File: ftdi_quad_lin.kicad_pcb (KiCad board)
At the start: 2 copper layers, 55 x 80 mm, 142 parts, among them J1 USB_C_Receptacle_USB2.0_16P, J2 Screw_Terminal_01x03, J3 Screw_Terminal_01x03, J4 Screw_Terminal_01x03, J5 Screw_Terminal_01x03, J6 Conn_01x10, J7 Conn_01x05, J8 Barrel_Jack_MountingPin, Q1 MMBT2222A, Q10 MMBT2222A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

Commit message: pulldown reset
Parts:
- added R46: 100k, Resistor_SMD:R_0805_2012Metric, F.Cu at (100.2, 98.7)
- D10, D11, D12, D13: footprint Diode_SMD:D_SOD-323 -> Diode_SMD:D_SOD-323_HandSoldering
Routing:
- net Net-(JP9-A): track 6.77 -> 9.76 mm
- net GND: vias 118 -> 117

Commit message: fixin mes g
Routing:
- net GND: track 127.7 -> 131.6 mm, vias 117 -> 120
- net /LIN0_TXD: track 54.2 -> 56.5 mm
- net Net-(D15-K): track 61.5 -> 59.8 mm
- net /LIN0_RXD: track 52.8 -> 53.4 mm
- net /LIN2_TXD: track 66.0 -> 65.8 mm, vias 4 -> 2

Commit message: power checked
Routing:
- net +5V: track 274.6 -> 283.5 mm
- net Net-(D15-K): track 59.8 -> 59.2 mm
- net GND: track 131.6 -> 131.3 mm, vias 120 -> 116
- added copper zone on F.Cu, net +12V
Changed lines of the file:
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@@
 	)
 	(segment
+		(start 86.6 65.275)
+		(end 85.1 66.775)
+		(width 0.5)
+		(layer "F.Cu")
+		(net 8)
+	)
+	(segment
 		(start 109.225 73)
 		(end 110.049311 72.175689)
@@
 	)
 	(segment
+		(start 93.35 65.275)
+		(end 91.3875 65.275)
+		(width 0.5)
+		(layer "F.Cu")
+		(net 8)
+	)
+	(segment
 		(start 97.36759 85.08241)
 		(end 97.1 85.35)
@@
 	)
 	(segment
+		(start 91.3875 65.275)
+		(end 89.8875 66.775)
+		(width 0.5)
+		(layer "F.Cu")
+		(net 8)
+	)
+	(segment
 		(start 94.86759 88.08241)
 		(end 97.36759 90.58241)
@@
 	)
 	(segment
-		(start 91.3875 65.275)
-		(end 89.8875 66.775)
-		(width 0.2)
-		(layer "F.Cu")
-		(net 8)
-	)
-	(segment
 		(start 119.1 94.121249)
 		(end 119.1 91.48625)
@@
 	)
 	(segment
-		(start 93.35 65.275)
-		(end 91.3875 65.275)
-		(width 0.2)
-		(layer "F.Cu")
-		(net 8)
-	)
-	(segment
 		(start 85.1 66.775)
 		(end 84.14491 67.73009)
@@
 	)
 	(segment
+		(start 93.35 65.275)
+		(end 86.6 65.275)
+		(width 0.5)
+		(layer "F.Cu")
+		(net 8)
+	)
+	(segment
 		(start 104.4 45.2)
 		(end 102.2 45.2)
@@
 	)
 	(segment
-		(start 89.02 69.395552)
-		(end 89.02 69.05)
-		(width 0.2)
-		(layer "F.Cu")
-		(net 10)
-	)
-	(segment
 		(start 87.215552 71.2)
 		(end 89.02 69.395552)
@@
 	)
 	(via
-		(at 98.4 50.6)
-		(size 0.6)
-		(drill 0.3)
-		(layers "F.Cu" "B.Cu")
-		(free yes)
-		(net 10)
-	)
-	(via
 		(at 123.6 81.8)
 		(size 0.6)
@@
 	)
 	(via
-		(at 98.4 61.2)
-		(size 0.6)
-		(drill 0.3)
-		(layers "F.Cu" "B.Cu")
-		(free yes)
-		(net 10)
-	)
-	(via
-		(at 91 58.8)
-		(size 0.6)
-		(drill 0.3)
-		(layers "F.Cu" "B.Cu")
-		(free yes)
-		(net 10)
-	)
-	(via
 		(at 83 90.2)
 		(size 0.6)
@@
 	)
 	(via
-		(at 91 52.2)
-		(size 0.6)
-		(drill 0.3)
-		(layers "F.Cu" "B.Cu")
-		(free yes)
-		(net 10)
-	)
-	(via
 		(at 82.8 77.6)
 		(size 0.6)
@@
 	(segment
 		(start 102.02241 109.72759)
-		(end 102.02241 101.6)
+		(end 102.02241 96.22241)
 		(width 0.2)
 		(layer "F.Cu")
@@
 	)
 	(segment
-		(start 102.02241 101.6)
-		(end 102.02241 96.22241)
-		(width 0.2)
-		(layer "F.Cu")
-		(net 80)
-	)
-	(segment
 		(start 98.175 92.08241)
 		(end 98.175 92.249214)
@@
 	)
 	(segment
-		(start 100.977334 84.13241)
-		(end 101.922462 85.077538)
-		(width 0.2)
-		(layer "F.Cu")
-		(net 82)
-	)
-	(segment
 		(start 93.75 82.65741)
 		(end 93.75 83.46482)
@@
 	)
 	(segment
-		(start 101.922462 85.077538)
+		(start 100.977334 84.13241)
 		(end 102.522462 85.677538)
 		(width 0.2)
@@
 	)
 	(segment
-		(start 113.565 104.95)
-		(end 113.35 104.95)
-		(width 0.2)
-		(layer "F.Cu")
-		(net 93)
-	)
-	(segment
 		(start 112.579883 103.819966)
 		(end 112.579883 103.964883)
@@
 	)
 	(segment
-		(start 111.35147 101.2)
-		(end 111.6 101.2)
-		(width 0.2)
-		(layer "B.Cu")
-		(net 126)
-	)
-	(segment
 		(start 111.2 101.2)
 		(end 111.6 101.2)
@@
 	)
 	(segment
-		(start 113.6 82.65)
-		(end 113.05 82.65)
-		(width 0.2)
-		(layer "F.Cu")
-		(net 127)
-	)
-	(segment
 		(start 105.65 78.20147)
 		(end 105.65 77.6)
@@
 	)
 	(zone
+		(net 88)
+		(net_name "+12V")
+		(layer "F.Cu")
+		(hatch edge 0.5)
+		(priority 1)
+		(connect_pads
+			(clearance 0.5)
+		)
+		(min_thickness 0.25)
+		(filled_areas_thickness no)
+		(fill yes
+			(thermal_gap 0.5)
+			(thermal_bridge_width 0.5)
+		)
+		(polygon
+			(pts
+				(xy 98.4 50.6) (xy 91 50.6) (xy 91 61.2) (xy 98.4 61.2)
+			)
+		)
+	)
+	(zone

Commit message: updated libs
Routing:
- net GND: vias 116 -> 121
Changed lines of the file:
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@@
 			)
 		)
+		(property "manf#" "B3B-XH-A (LF)(SN)"
+			(at 0 0 -90)
+			(layer "F.SilkS")
+			(hide yes)
+			(effects
+				(font
+					(size 1 1)
+					(thickness 0.1)
+				)
+			)
+		)
 		(property ki_fp_filters "TerminalBlock*:*")
 		(sheetname "LIN 2")
@@
 			)
 		)
+		(property "manf#" "B3B-XH-A (LF)(SN)"
+			(at 0 0 -90)
+			(layer "F.SilkS")
+			(hide yes)
+			(effects
+				(font
+					(size 1 1)
+					(thickness 0.1)
+				)
+			)
+		)
 		(property ki_fp_filters "TerminalBlock*:*")
 		(sheetname "LIN 3")
@@
 			)
 		)
+		(property "manf#" "B3B-XH-A (LF)(SN)"
+			(at 0 0 -90)
+			(layer "F.SilkS")
+			(hide yes)
+			(effects
+				(font
+					(size 1 1)
+					(thickness 0.1)
+				)
+			)
+		)
 		(property ki_fp_filters "TerminalBlock*:*")
 		(sheetname "LIN 0")
@@
 			)
 		)
+		(property "manf#" "1216.1002"
+			(at 0 0 90)
+			(layer "F.SilkS")
+			(hide yes)
+			(effects
+				(font
+					(size 1 1)
+					(thickness 0.1)
+				)
+			)
+		)
 		(property ki_fp_filters "LED* LED_SMD:* LED_THT:*")
 		(sheetname "leds_indication")
@@
 			)
 		)
+		(property "manf#" "1216.1002"
+			(at 0 0 90)
+			(layer "F.SilkS")
+			(hide yes)
+			(effects
+				(font
+					(size 1 1)
+					(thickness 0.1)
+				)
+			)
+		)
 		(property ki_fp_filters "LED* LED_SMD:* LED_THT:*")
 		(sheetname "leds_indication")
@@
 			)
 		)
+		(property "manf#" "1216.1002"
+			(at 0 0 90)
+			(layer "F.SilkS")
+			(hide yes)
+			(effects
+				(font
+					(size 1 1)
+					(thickness 0.1)
+				)
+			)
+		)
 		(property ki_fp_filters "LED* LED_SMD:* LED_THT:*")
 		(sheetname "leds_indication")
@@
 			)
 		)
+		(property "manf#" "B3B-XH-A (LF)(SN)"
+			(at 0 0 -90)
+			(layer "F.SilkS")
+			(hide yes)
+			(effects
+				(font
+					(size 1 1)
+					(thickness 0.1)
+				)
+			)
+		)
 		(property ki_fp_filters "TerminalBlock*:*")
 		(sheetname "LIN 1")
@@
 			)
 		)
+		(property "manf#" "1216.1002"
+			(at 0 0 90)
+			(layer "F.SilkS")
+			(hide yes)
+			(effects
+				(font
+					(size 1 1)
+					(thickness 0.1)
+				)
+			)
+		)
 		(property ki_fp_filters "LED* LED_SMD:* LED_THT:*")
 		(sheetname "leds_indication")
@@
 	)
 	(via
+		(at 103 75)
+		(size 0.6)
+		(drill 0.3)
+		(layers "F.Cu" "B.Cu")
+		(free yes)
+		(net 10)
+	)
+	(via
 		(at 103.703619 51.980284)
 		(size 0.6)
@@
 	)
 	(via
-		(at 124 120.6)
+		(at 124 120.4)
 		(size 0.6)
 		(drill 0.3)
@@
 	)
 	(via
+		(at 88.8 43.8)
+		(size 0.6)
+		(drill 0.3)
+		(layers "F.Cu" "B.Cu")
+		(free yes)
+		(net 10)
+	)
+	(via
 		(at 120.6 111.4)
 		(size 0.6)
@@
 	)
 	(via
+		(at 132.8 65.8)
+		(size 0.6)
+		(drill 0.3)
+		(layers "F.Cu" "B.Cu")
+		(free yes)
+		(net 10)
+	)
+	(via
 		(at 88.272499 67.327501)
 		(size 0.6)
@@
 	)
 	(via
-		(at 120.8 120.4)
+		(at 121.6 120.4)
 		(size 0.6)
 		(drill 0.3)
@@
 	)
 	(via
+		(at 101.8 76.6)
+		(size 0.6)
+		(drill 0.3)
+		(layers "F.Cu" "B.Cu")
+		(free yes)
+		(net 10)
+	)
+	(via
 		(at 125.2 104)
 		(size 0.6)
@@
 	)
 	(via
-		(at 127.6 120.6)
+		(at 126.8 120.4)
 		(size 0.6)
 		(drill 0.3)
@@
 	)
 	(via
+		(at 133 97.8)
+		(size 0.6)
+		(drill 0.3)
+		(layers "F.Cu" "B.Cu")
+		(free yes)
+		(net 10)
+	)
+	(via
 		(at 130.2 57.2)
 		(size 0.6)
@@
 	)
 	(via
-		(at 118.2 121)
+		(at 118.6 120.4)
 		(size 0.6)
 		(drill 0.3)

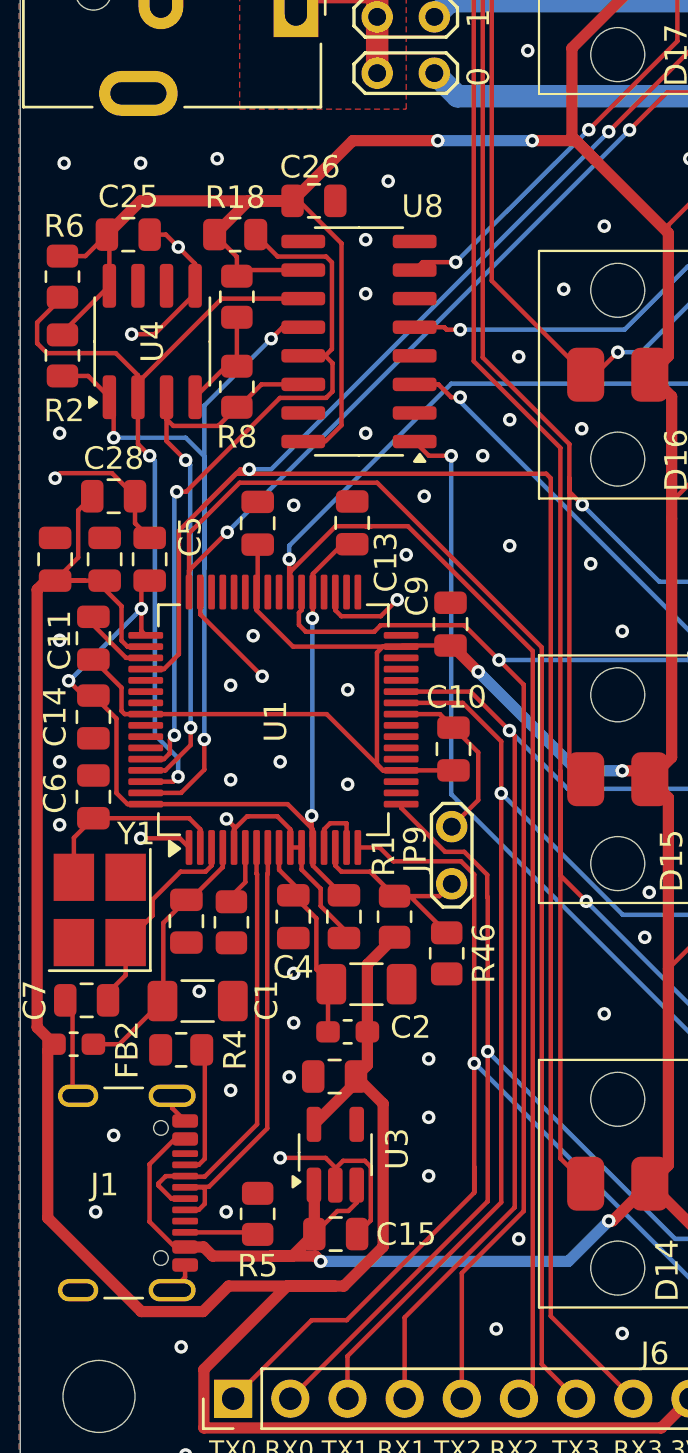
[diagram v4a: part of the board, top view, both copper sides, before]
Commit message: more capacitors
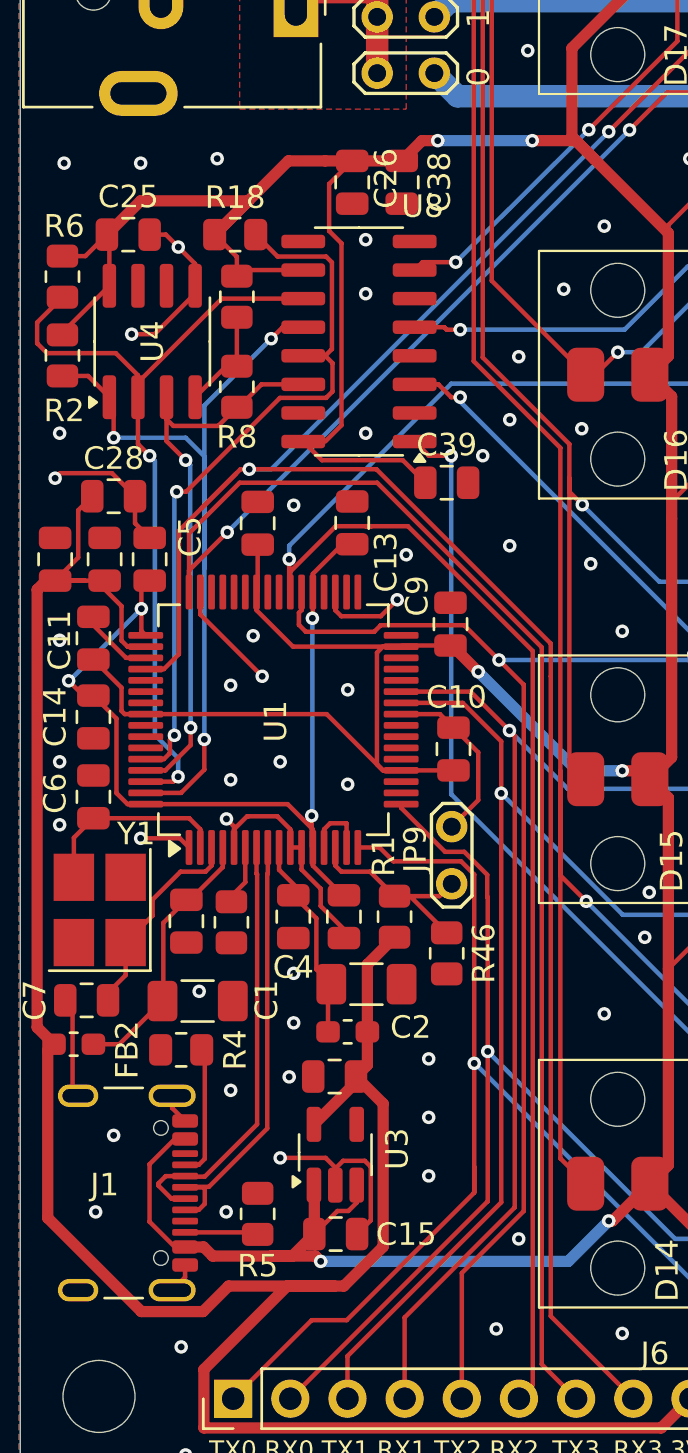
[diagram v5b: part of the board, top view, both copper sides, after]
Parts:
- added C38: 100nF, Capacitor_SMD:C_0805_2012Metric, F.Cu at (98.2, 64.5)
- added C39: 100nF, Capacitor_SMD:C_0805_2012Metric, F.Cu at (100.2, 77.8)
- moved C26 1.89 mm to (96.0, 64.5), turned to -90 degrees
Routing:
- net /LIN3_RXD: track 106.5 -> 101.7 mm
- net +5V: track 283.5 -> 284.8 mm
- net GND: vias 121 -> 119

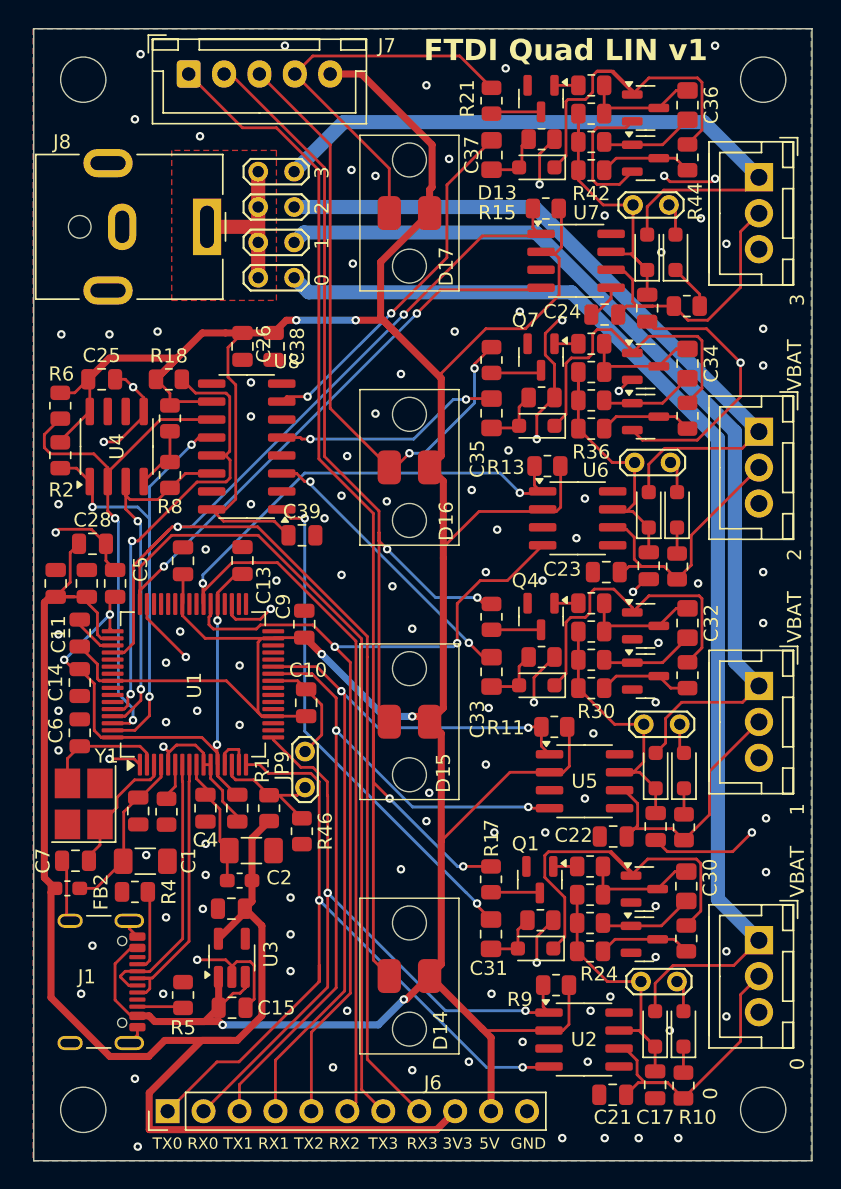
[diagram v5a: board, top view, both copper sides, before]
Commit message: more capacitors
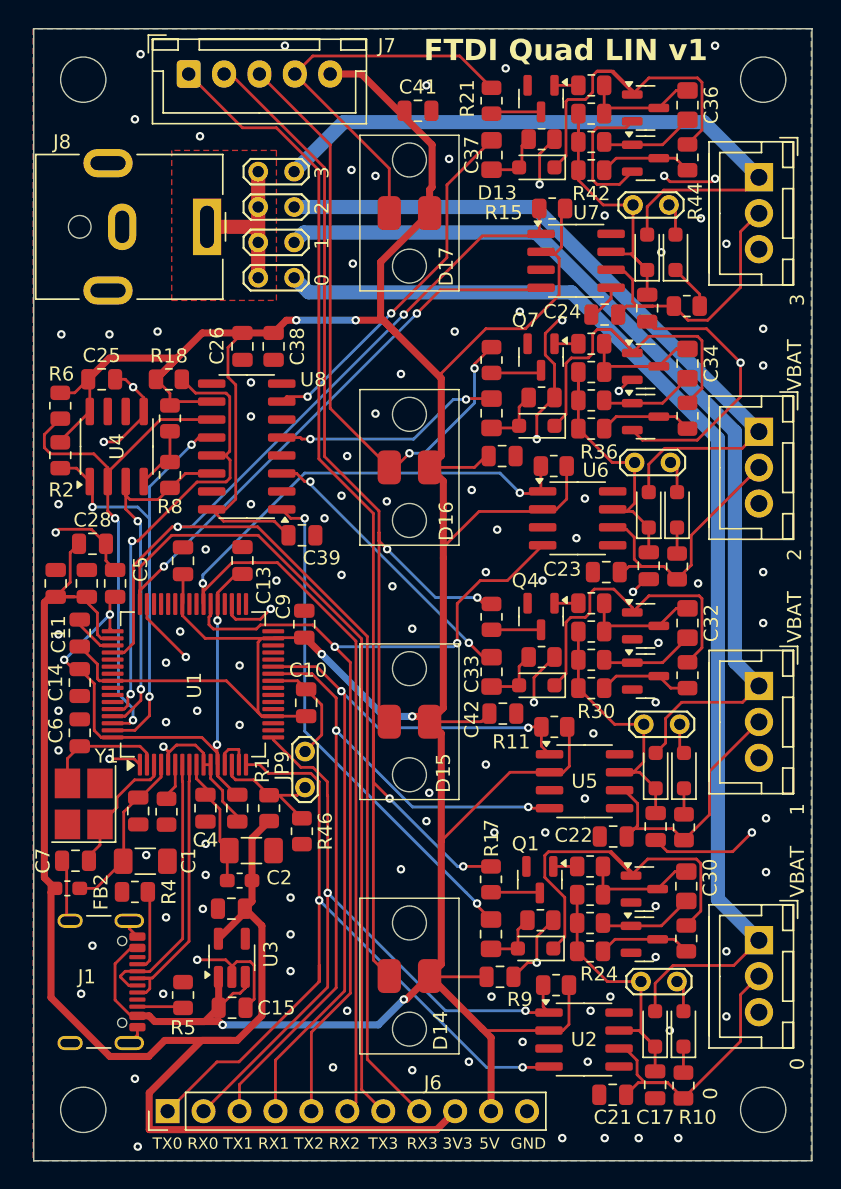
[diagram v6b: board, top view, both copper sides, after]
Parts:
- added C40: 100nF, Capacitor_SMD:C_0805_2012Metric, F.Cu at (114.3, 72.2)
- added C41: 100nF, Capacitor_SMD:C_0805_2012Metric, F.Cu at (108.4, 47.8)
- added C42: 100nF, Capacitor_SMD:C_0805_2012Metric, F.Cu at (114.4, 90.4)
- added C43: 100nF, Capacitor_SMD:C_0805_2012Metric, F.Cu at (114.2, 109.0)
- moved R13 0.45 mm to (118.0, 72.9)
- moved R15 0.45 mm to (117.9, 54.7)
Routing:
- net +5V: track 284.8 -> 297.6 mm
- net /LIN3_RXD: track 101.7 -> 99.0 mm
- net GND: track 131.3 -> 133.4 mm, vias 119 -> 117
- net /LIN2_RXD: track 80.5 -> 80.0 mm

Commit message: added ESD protection to lin
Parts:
- added D18: ESD1LIN24, Diode_SMD:D_SOD-323_HandSoldering, F.Cu at (130.6, 97.8)
- added D19: ESD1LIN24, Diode_SMD:D_SOD-323_HandSoldering, F.Cu at (130.6, 79.6)
- added D20: ESD1LIN24, Diode_SMD:D_SOD-323_HandSoldering, F.Cu at (131.2, 61.8)
- added D9: ESD1LIN24, Diode_SMD:D_SOD-323_HandSoldering, F.Cu at (126.0, 119.6)
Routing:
- net GND: track 133.4 -> 135.6 mm
- net /LIN 0/LIN: track 20.3 -> 22.3 mm
- net /LIN 2/LIN: track 20.0 -> 20.8 mm
